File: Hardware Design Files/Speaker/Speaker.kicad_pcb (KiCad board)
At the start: 2 copper layers, 40.2 x 36.1 mm, 22 parts, among them J1 D7-D0, J2 CLK DAC1 DAC2 PRE_AMP SPKR+ S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, J3 SPKR- SPKR+ 3V3 GND 5V D3V3 D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, U1 LMV358IDR, U2 MAX5187BEEG+, U3 PAM8304, U4 PAM8304, U5 PAM8304

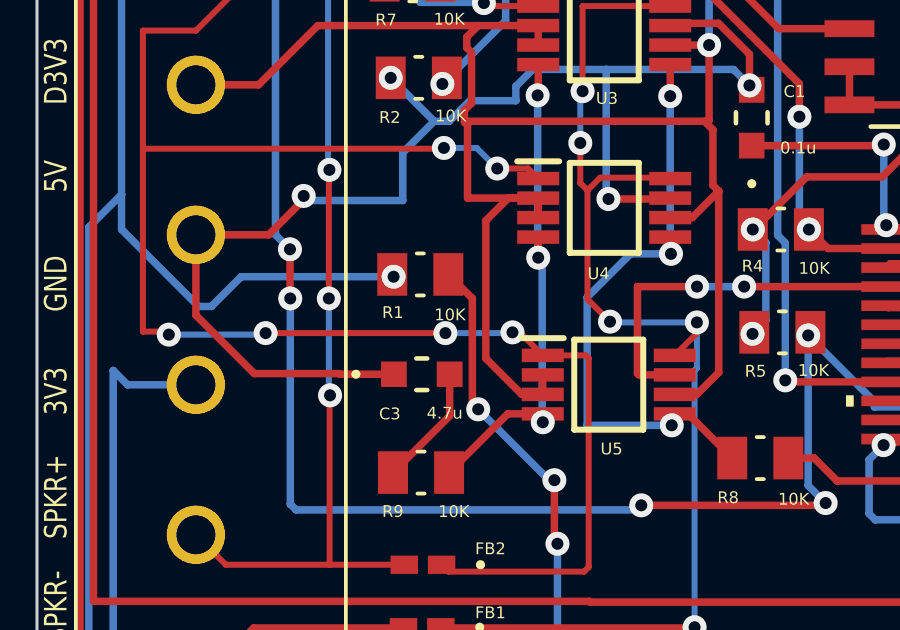
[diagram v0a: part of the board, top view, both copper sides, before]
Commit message: changed R1
changed from 10k to 70k such that chip select current ~5ua
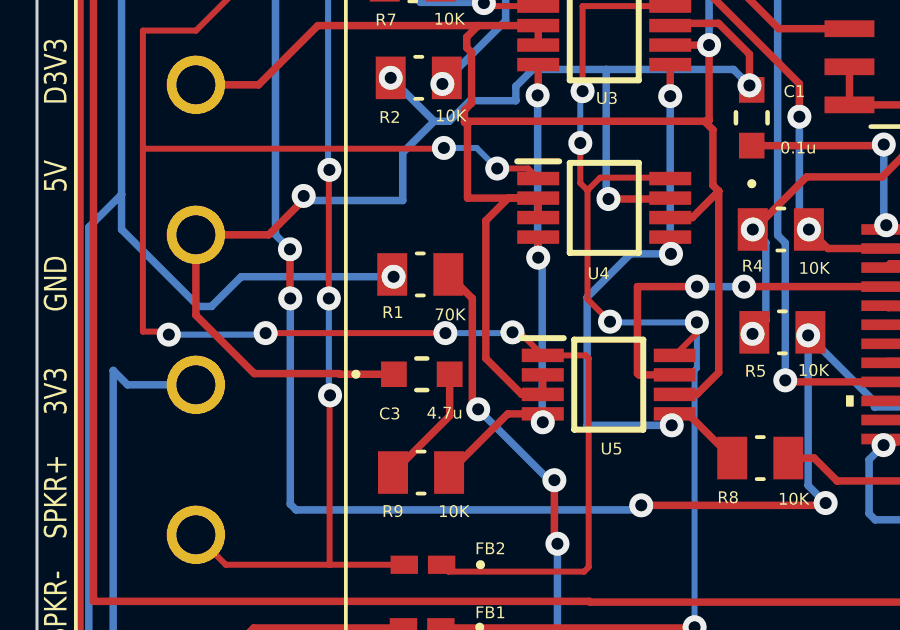
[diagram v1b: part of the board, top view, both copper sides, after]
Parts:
- R1: value 10K -> 70K
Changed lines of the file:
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@@
         (effects (font (size 0.393701 0.393701) (thickness 0.15)))
     )
-    (fp_text value "10K" (at 0.9906 1.3462) (layer "F.SilkS")
+    (fp_text value "70K" (at 0.9906 1.3462) (layer "F.SilkS")
         (effects (font (size 0.393701 0.393701) (thickness 0.098425)))
     )
